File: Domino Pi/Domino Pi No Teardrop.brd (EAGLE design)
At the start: 71.1 x 33 mm, 77 parts, among them J1 MH28-1, J2 MH28-1, M1 DOMINO, SW1 IT-1210, U1 MP65151DJ, U2 MP2162GQH, U3 CP2104-F03-GM, U4 74LVC1G125DCK

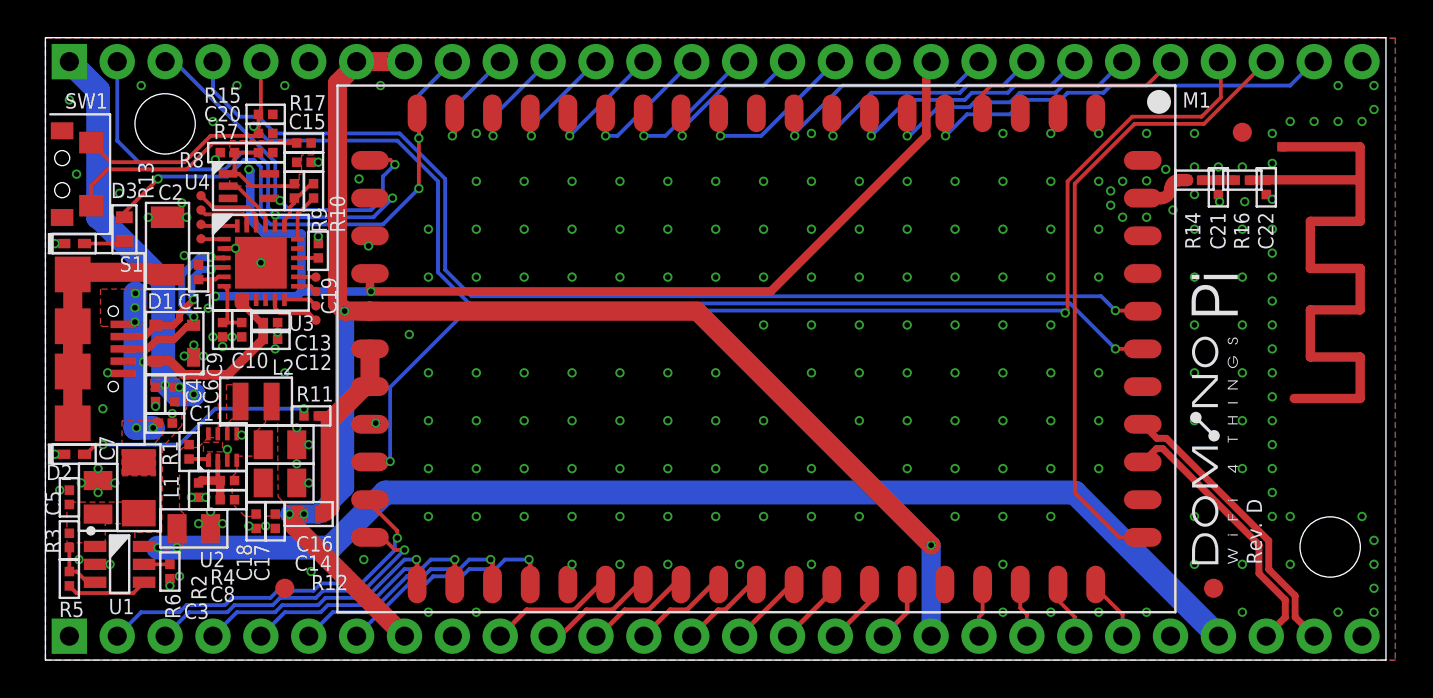
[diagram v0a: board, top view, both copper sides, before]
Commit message: Domnio Pi Rev. E: changed silkscreen font ratio to 20%
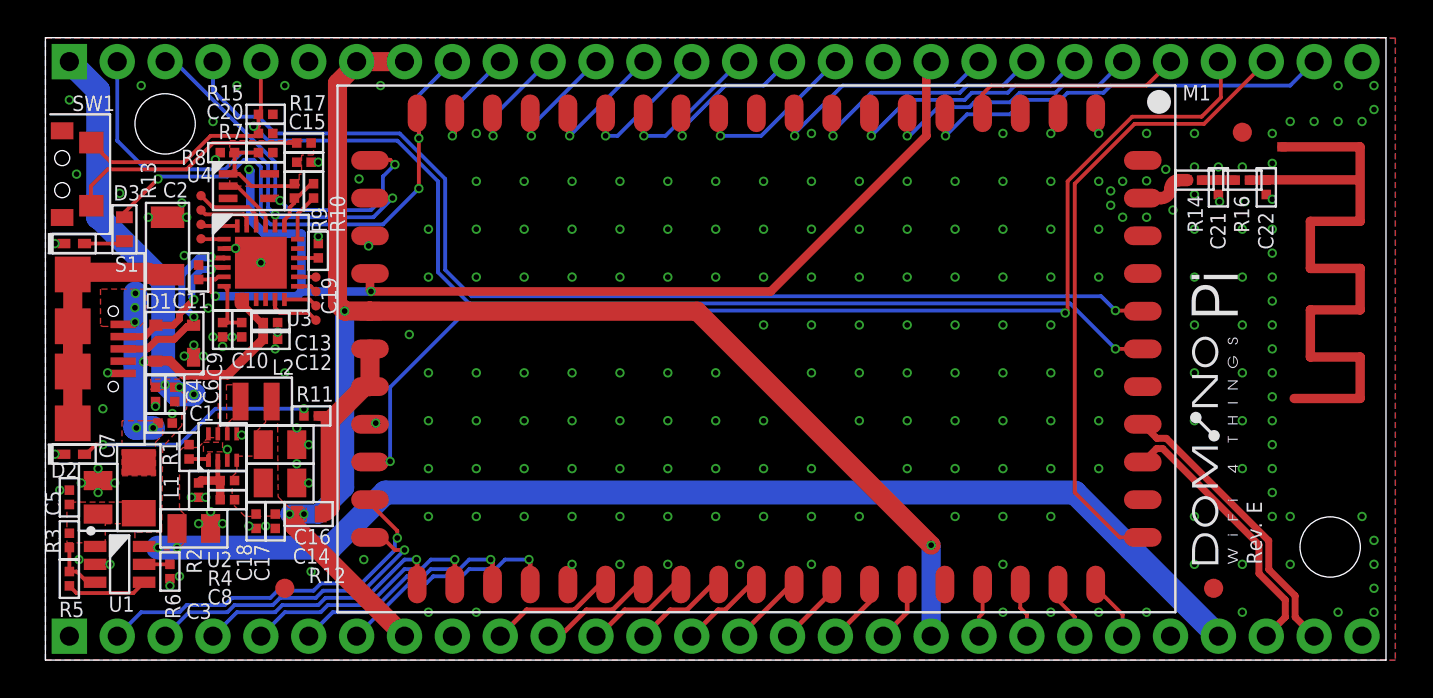
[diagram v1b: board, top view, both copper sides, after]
